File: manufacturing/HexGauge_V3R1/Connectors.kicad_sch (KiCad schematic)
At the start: 17 parts, among them J1 USB_B_Micro, J2 Conn_ARM_SWD_TC2030-NL, J3 Micro_SD_Card, J4 Conn_01x04_Pin, SW2 SW_Omron_B3FS, U4 USBLC6-4

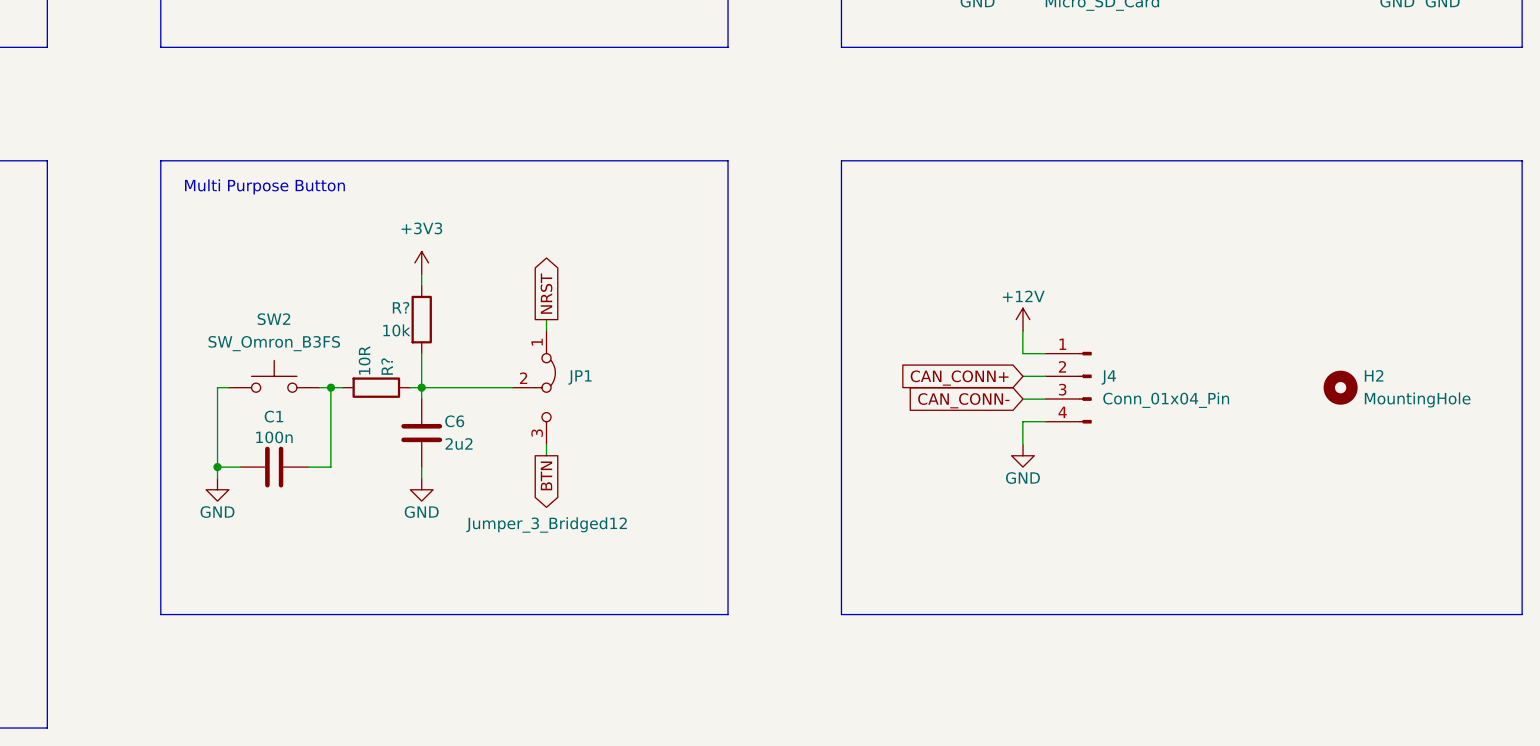
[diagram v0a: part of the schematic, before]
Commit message: Cleaned Up Schematic
Added Blockdiagram
Reannotated Symbols
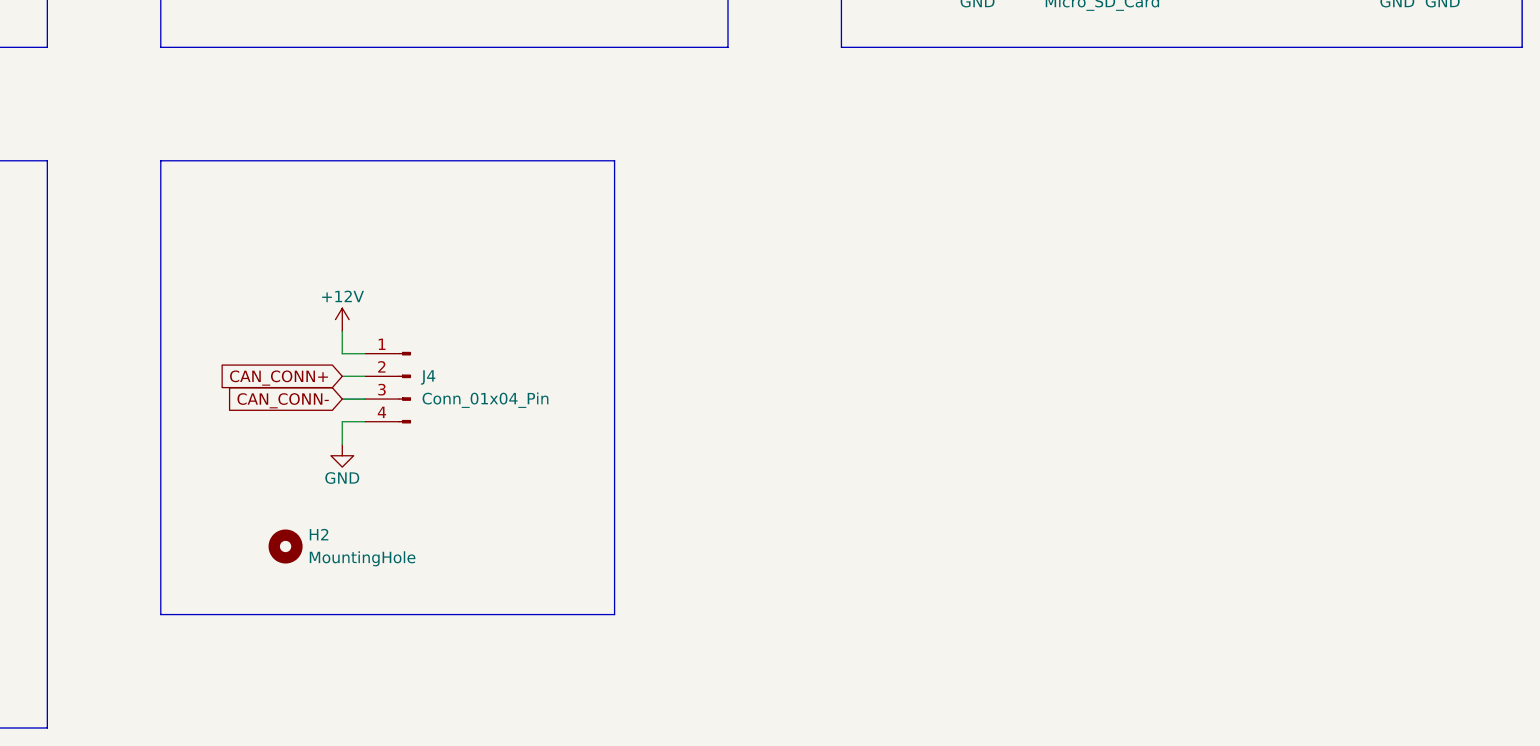
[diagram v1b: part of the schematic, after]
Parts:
- removed C1: 100n, Capacitor_SMD:C_0402_1005Metric, symbol Device:C
- removed C6: 2u2, Capacitor_SMD:C_0603_1608Metric, symbol Device:C
- removed JP1: Jumper_3_Bridged12, Jumper:SolderJumper-3_P1.3mm_Open_RoundedPad1.0x1.5mm, symbol Jumper:Jumper_3_Bridged12
- removed R?: 10k, Resistor_SMD:R_0402_1005Metric, symbol Device:R
- removed R?: 10R, Resistor_SMD:R_0402_1005Metric, symbol Device:R
- removed SW2: SW_Omron_B3FS, Button_Switch_SMD:Panasonic_EVQPUL_EVQPUC, symbol Switch:SW_Omron_B3FS
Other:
- note removed: "Multi Purpose Button"
- moved on the sheet: H2, J4
